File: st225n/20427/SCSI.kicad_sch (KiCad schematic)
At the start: 27 parts, among them J8 SCSI, J9 SCSI ID, U11 74LS240, U12 74LS240, U13 74F08, U14 74LS14, U15 74F38, U16 74F38, U17 74F38, U18 74F38, U19 74LS373, U20 7406, U25 74F04, U26 74LS00, U29 74LS123, U5 AIC-010L, U6 AIC-300L, U7 SRAM_6116

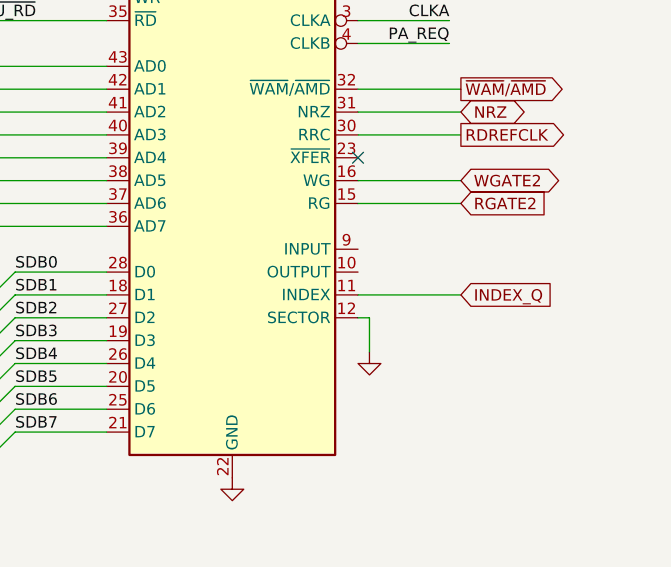
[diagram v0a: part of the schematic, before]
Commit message: Add component values. SRAM tweak.
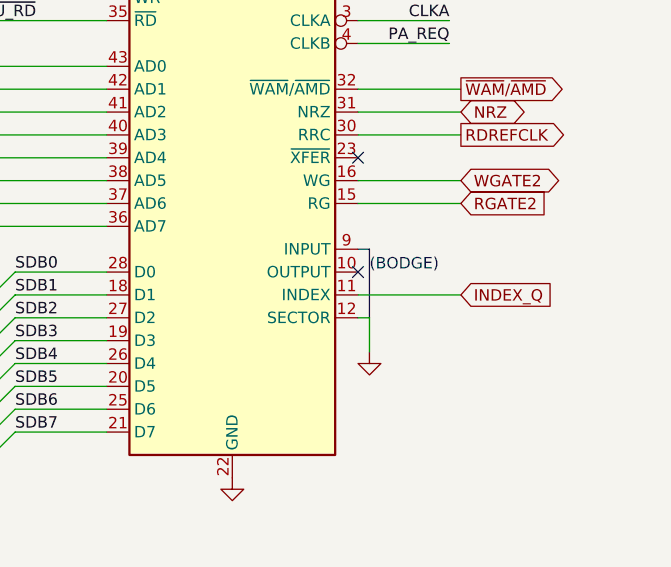
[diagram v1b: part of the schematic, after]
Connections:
- no-connect marks 18 -> 19
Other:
- note added: "(BODGE)"
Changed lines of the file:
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@@
   (no_connect (at 109.22 170.18))
   (no_connect (at 220.98 260.35))
+  (no_connect (at 373.38 208.28))
   (no_connect (at 195.58 270.51))
   (no_connect (at 134.62 167.64))
@@
     (stroke (width 0) (type default))
   )
+  (polyline (pts (xy 374.65 205.74) (xy 374.65 213.36))
+    (stroke (width 0) (type default) (color 255 0 255 1))
+  )
   (wire (pts (xy 121.92 189.23) (xy 121.92 191.77))
     (stroke (width 0) (type default))
@@
   (wire (pts (xy 83.82 231.14) (xy 83.82 218.44))
     (stroke (width 0) (type default))
+  )
+  (polyline (pts (xy 373.38 205.74) (xy 374.65 205.74))
+    (stroke (width 0) (type default) (color 255 0 255 1))
   )
   (wire (pts (xy 373.38 200.66) (xy 384.81 200.66))
@@
     (effects (font (size 1.27 1.27)) (justify left bottom))
   )
+  (text "(BODGE)" (at 374.65 208.28 0)
+    (effects (font (size 1.27 1.27)) (justify left bottom))
+  )
